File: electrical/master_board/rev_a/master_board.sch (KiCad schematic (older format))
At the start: 4 parts

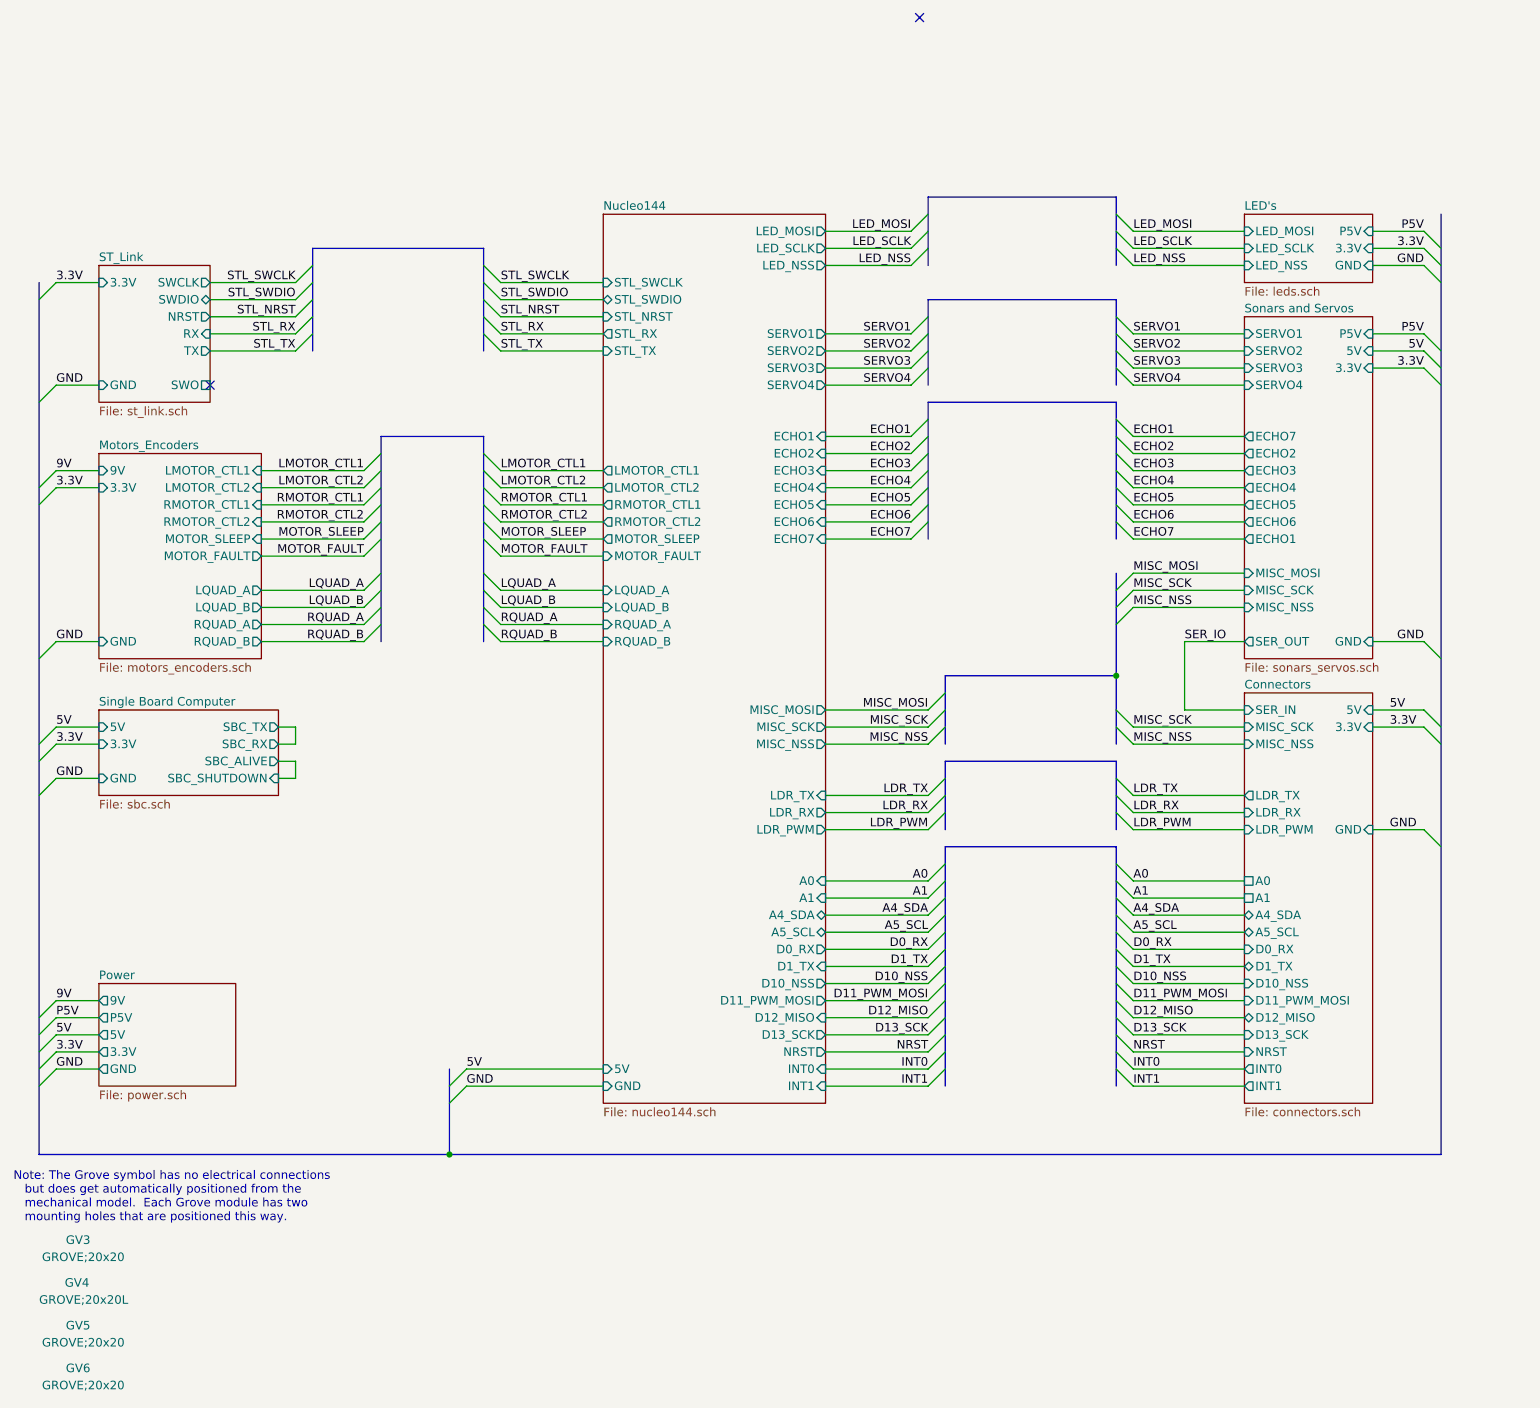
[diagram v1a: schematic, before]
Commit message: Cleaned up schematics some.
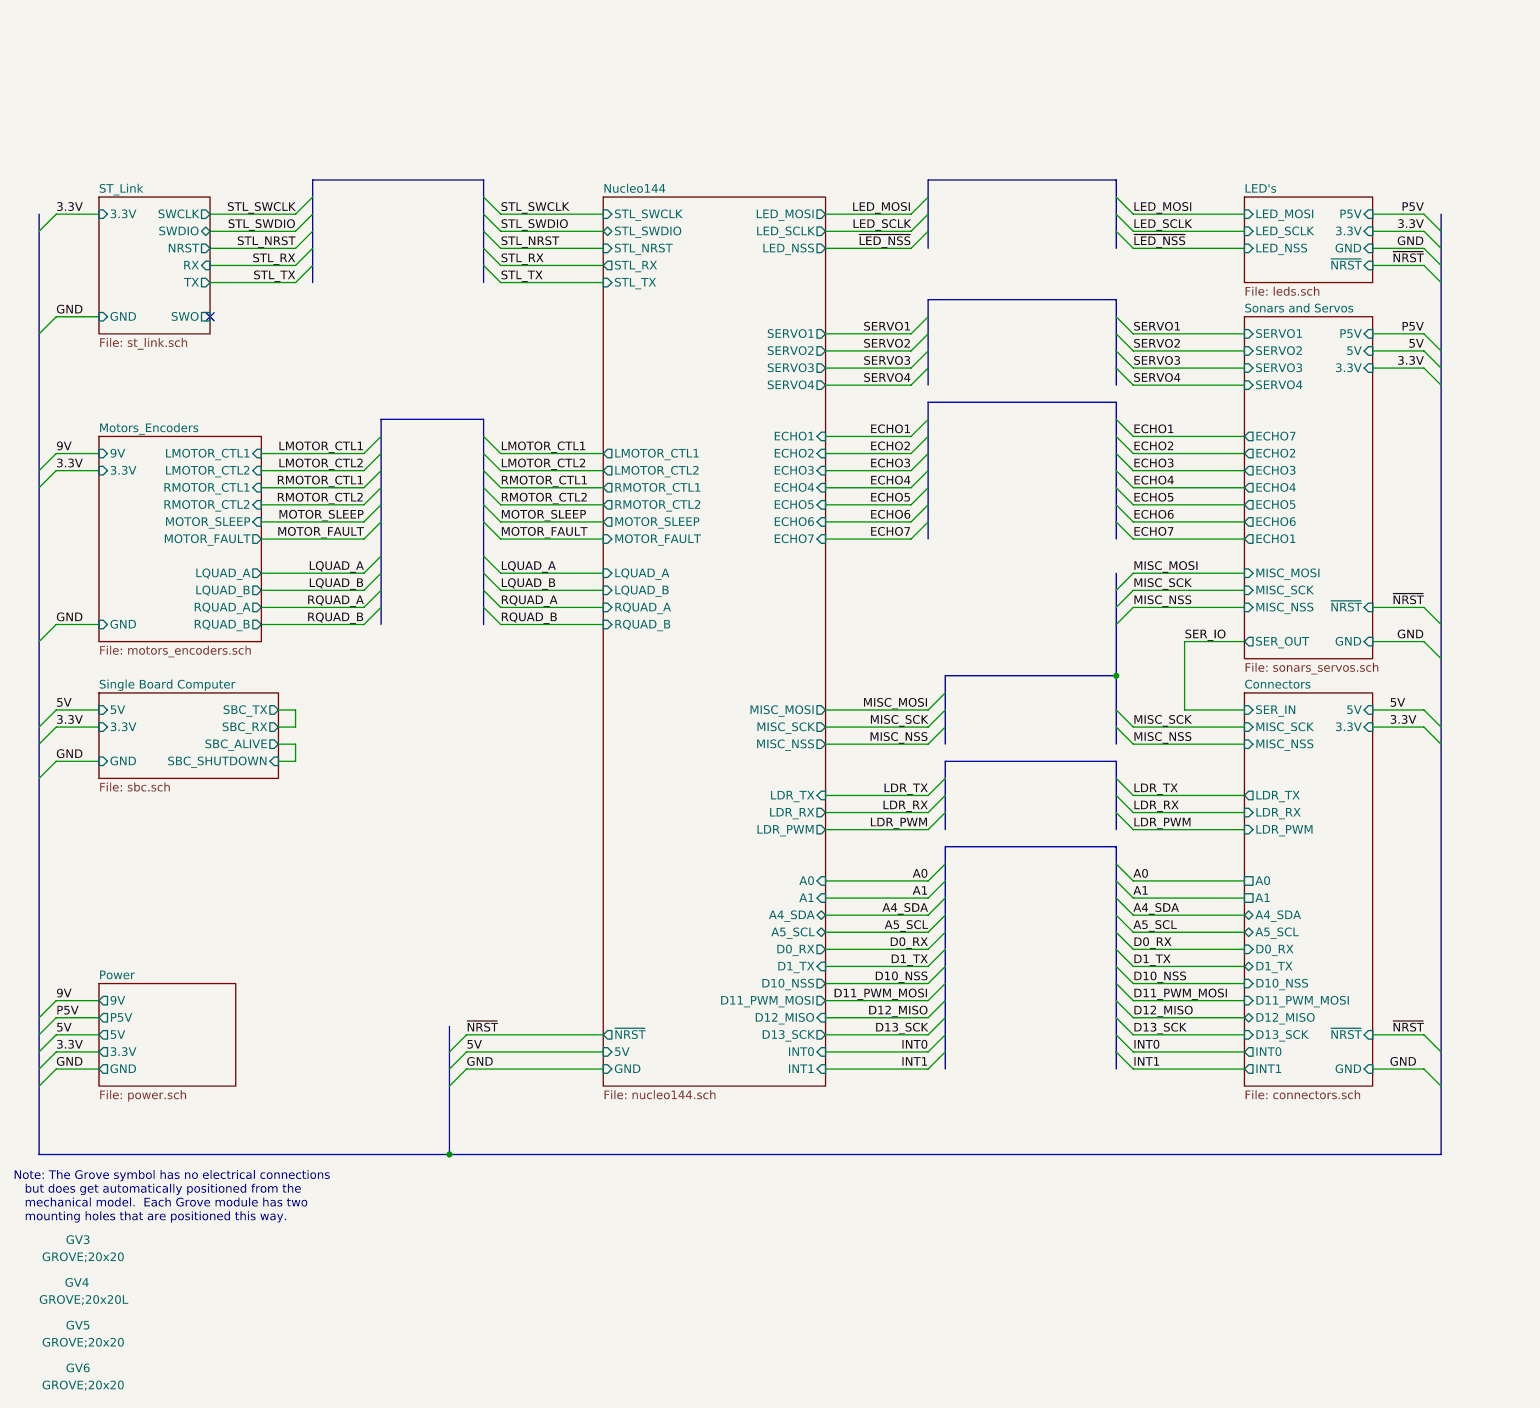
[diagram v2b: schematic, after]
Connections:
- no-connect marks 2 -> 1

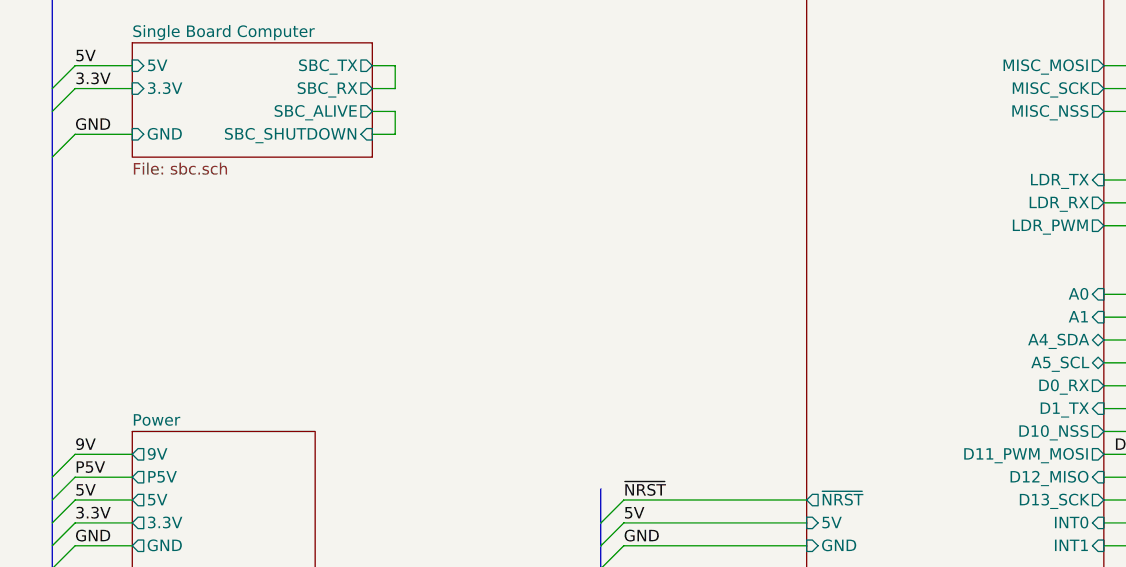
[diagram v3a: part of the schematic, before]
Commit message: Added WOWBus Schematic Sheet.
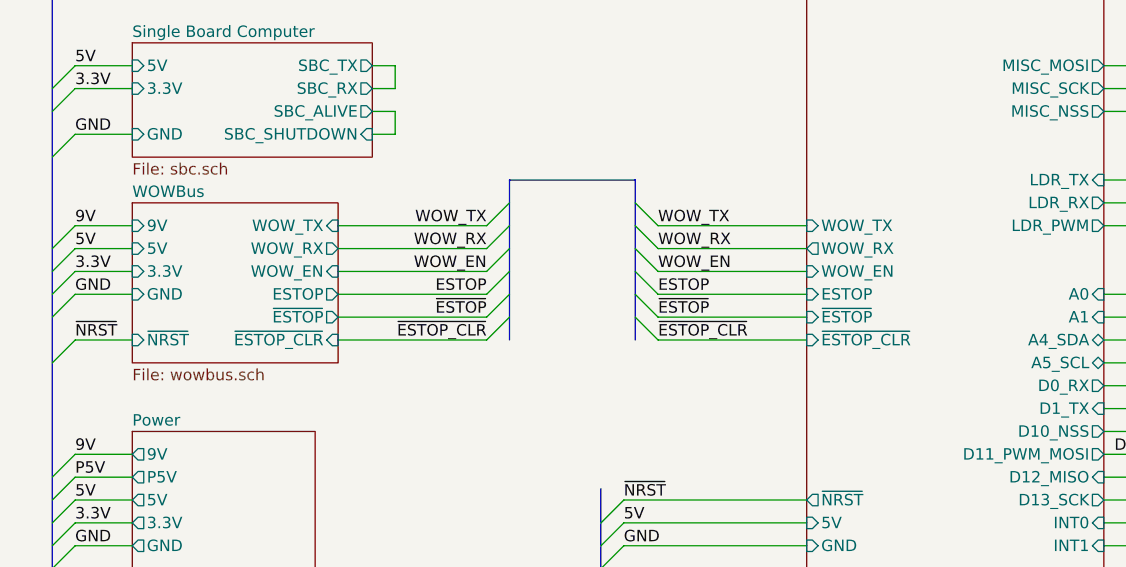
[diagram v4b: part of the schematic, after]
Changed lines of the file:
@@
 $Descr A 11000 8500
 encoding utf-8
-Sheet 1 9
-Title "HR2 Sonars and Servos"
-Date "2020-10-03"
+Sheet 1 10
+Title "HR2 Overview"
+Date "2020-10-17"
 Rev "A"
 Comp "HomeBrew Robotics Club"
@@
 F50 "INT1" I R 5400 6000 50
 F51 "LED_NSS" O R 5400 1200 50
+F52 "WOW_TX" I L 4100 4600 50
+F53 "WOW_RX" O L 4100 4700 50
+F54 "WOW_EN" I L 4100 4800 50
+F55 "ESTOP" I L 4100 4900 50
+F56 "~ESTOP" I L 4100 5000 50
+F57 "~ESTOP_CLR" I L 4100 5100 50
 $EndSheet
 Wire Wire Line
@@
 Text Label 8900 3300 2    50   ~ 0
 ~NRST
+$Sheet
+S 1150 4500 900  700
+U 5F8C2F57
+F0 "WOWBus" 50
+F1 "wowbus.sch" 50
+F2 "9V" I L 1150 4600 50
+F3 "GND" I L 1150 4900 50
+F4 "WOW_EN" I R 2050 4800 50
+F5 "3.3V" I L 1150 4800 50
+F6 "5V" I L 1150 4700 50
+F7 "WOW_TX" I R 2050 4600 50
+F8 "WOW_RX" O R 2050 4700 50
+F9 "ESTOP" O R 2050 4900 50
+F10 "~ESTOP" O R 2050 5000 50
+F11 "~ESTOP_CLR" I R 2050 5100 50
+F12 "~NRST" I L 1150 5100 50
+$EndSheet
+Wire Wire Line
+	900  4600 1150 4600
+Wire Wire Line
+	900  4700 1150 4700
+Entry Wire Line
+	900  5100 800  5200
+Entry Wire Line
+	900  4900 800  5000
+Entry Wire Line
+	900  4800 800  4900
+Entry Wire Line
+	900  4700 800  4800
+Entry Wire Line
+	900  4600 800  4700
+Wire Wire Line
+	900  4800 1150 4800
+Wire Wire Line
+	900  4900 1150 4900
+Wire Wire Line
+	900  5100 1150 5100
+Text Label 900  4800 0    50   ~ 0
+3.3V
+Text Label 900  4900 0    50   ~ 0
+GND
+Text Label 900  4600 0    50   ~ 0
+9V
+Text Label 900  4700 0    50   ~ 0
+5V
+Text Label 900  5100 0    50   ~ 0
+~NRST
+Entry Wire Line
+	2700 4600 2800 4500
+Entry Wire Line
+	2700 4700 2800 4600
+Entry Wire Line
+	2700 4800 2800 4700
+Entry Wire Line
+	2700 4900 2800 4800
+Entry Wire Line
+	2700 5000 2800 4900
+Entry Wire Line
+	2700 5100 2800 5000
+Wire Wire Line
+	2050 5100 2700 5100
+Wire Wire Line
+	2050 5000 2700 5000
+Wire Wire Line
+	2700 4900 2050 4900
+Wire Wire Line
+	2050 4800 2700 4800
+Wire Wire Line
+	2700 4700 2050 4700
+Wire Wire Line
+	2050 4600 2700 4600
+Text Label 2700 4600 2    50   ~ 0
+WOW_TX
+Text Label 2700 4700 2    50   ~ 0
+WOW_RX
+Text Label 2700 4800 2    50   ~ 0
+WOW_EN
+Text Label 2700 4900 2    50   ~ 0
+ESTOP
+Text Label 2700 5000 2    50   ~ 0
+~ESTOP
+Text Label 2700 5100 2    50   ~ 0
+~ESTOP_CLR
+Entry Wire Line
+	3450 4600 3350 4500
+Entry Wire Line
+	3450 4700 3350 4600
+Entry Wire Line
+	3450 4800 3350 4700
+Entry Wire Line
+	3450 4900 3350 4800
+Entry Wire Line
+	3450 5000 3350 4900
+Entry Wire Line
+	3450 5100 3350 5000
+Wire Wire Line
+	3450 5100 4100 5100
+Wire Wire Line
+	3450 5000 4100 5000
+Wire Wire Line
+	4100 4900 3450 4900
+Wire Wire Line
+	3450 4800 4100 4800
+Wire Wire Line
+	4100 4700 3450 4700
+Wire Wire Line
+	3450 4600 4100 4600
+Text Label 3450 4600 0    50   ~ 0
+WOW_TX
+Text Label 3450 4700 0    50   ~ 0
+WOW_RX
+Text Label 3450 4800 0    50   ~ 0
+WOW_EN
+Text Label 3450 4900 0    50   ~ 0
+ESTOP
+Text Label 3450 5000 0    50   ~ 0
+~ESTOP
+Text Label 3450 5100 0    50   ~ 0
+~ESTOP_CLR
+Wire Bus Line
+	2800 4400 3350 4400
 Wire Bus Line
 	7100 3700 7100 4100
@@
 	6000 1500 6000 2000
 Wire Bus Line
+	2800 4400 2800 5100
+Wire Bus Line
+	3350 4400 3350 5100
+Wire Bus Line
 	2800 2200 2800 3400
 Wire Bus Line
@@
 	3400 2200 3400 3400
 Wire Bus Line
+	9000 1000 9000 6500
+Wire Bus Line
+	7100 4700 7100 6000
+Wire Bus Line
+	6100 4700 6100 6000
+Wire Bus Line
 	800  1000 800  6500
-Wire Bus Line
-	9000 1000 9000 6500
-Wire Bus Line
-	7100 4700 7100 6000
-Wire Bus Line
-	6100 4700 6100 6000
 $EndSCHEMATC

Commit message: Wrapped up SBC sheet.
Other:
- note added: ""Arduino" Signals"
- note added: "LED Signals"
- note added: "LIDAR Signals"
- note added: "Miscellaneous I/O Signals"
- note added: "Motor/Encoder Signals"
- note added: "Power/Ground/Reset Signals"
- note added: "ST-Link Signals"
- note added: "Servo Signals"
- note added: "Single Board Computer Signals"
- note added: "Sonar Signals"
- note added: "WOWBus Signals"
